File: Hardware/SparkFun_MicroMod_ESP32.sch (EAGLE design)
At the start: 47 parts, among them J1 MICROMOD-2222, Q2 MBT3904DW1T1, U1 W25QXX128MBIT-6X5, U2 ESP32, U4 CP2102N, Y1 40MHz, Y2 32.768kHz

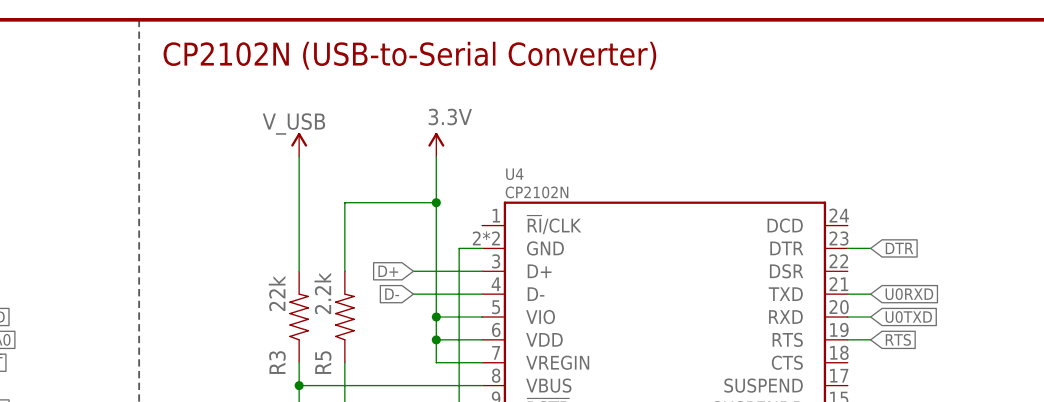
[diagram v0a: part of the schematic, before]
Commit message: Updated USB to UART
USB to UART converter can be either the CP2102N or CP2104
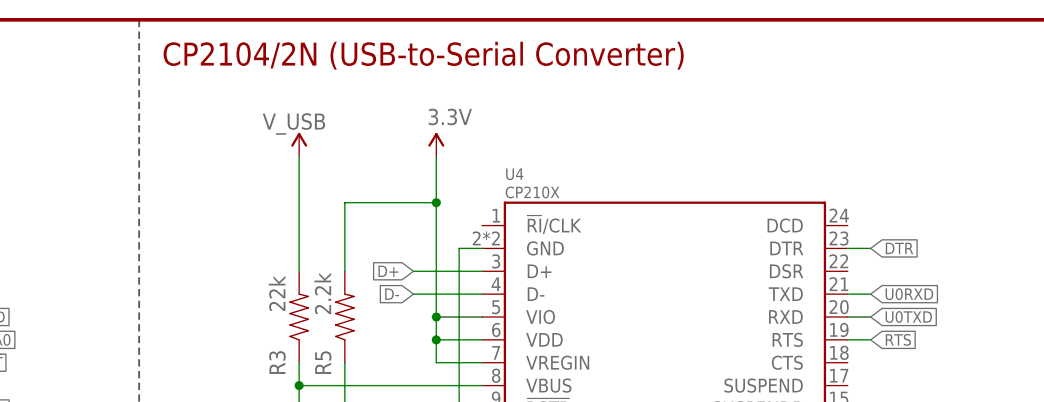
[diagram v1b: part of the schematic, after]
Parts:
- U4: value CP2102N -> CP210X
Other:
- note added: "CP2104/2N (USB-to-Serial Converter)"
- note removed: "CP2102N (USB-to-Serial Converter)"
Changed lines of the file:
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@@
 <?xml version="1.0" encoding="utf-8"?>
 <!DOCTYPE eagle SYSTEM "eagle.dtd">
-<eagle version="9.6.2">
+<eagle version="9.5.2">
 <drawing>
 <settings>
@@
 <layer number="255" name="routoute" color="7" fill="1" visible="yes" active="yes"/>
 </layers>
-<schematic xreflabel="%F%N/%S" xrefpart="1_/%S.%C%R">
+<schematic xreflabel="%F%N/%S" xrefpart="/%S.%C%R">
 <attributes>
 </attributes>
@@
 <part name="C27" library="SparkFun-Capacitors" deviceset="3.0NF" device="-0402T-50V-5%" value="3.0nF"/>
 <part name="GND40" library="SparkFun-PowerSymbols" deviceset="GND" device=""/>
-<part name="U4" library="SparkFun-IC-Comms" deviceset="CP2102N" device=""/>
+<part name="U4" library="SparkFun-IC-Comms" deviceset="CP2102N" device="" value="CP210X"/>
 <part name="GND1" library="SparkFun-PowerSymbols" deviceset="GND" device=""/>
 <part name="SUPPLY5" library="SparkFun-PowerSymbols" deviceset="3.3V" device=""/>
@@
 <text x="381" y="114.3" size="1.778" layer="97" font="vector" align="top-center">If DTR is LOW, toggling RTS from HIGH to LOW resets to run mode.
 If RTS is HIGH, toggling DTR from LOW to HIGH resets to bootloader.</text>
-<text x="332.74" y="274.32" size="2.54" layer="94" font="vector">CP2102N (USB-to-Serial Converter)</text>
+<text x="332.74" y="274.32" size="2.54" layer="94" font="vector">CP2104/2N (USB-to-Serial Converter)</text>
 <text x="200.66" y="274.32" size="2.54" layer="94" font="vector">MicroMod Connector</text>
 <wire x1="198.12" y1="279.4" x2="198.12" y2="193.04" width="0.2032" layer="97" style="longdash"/>

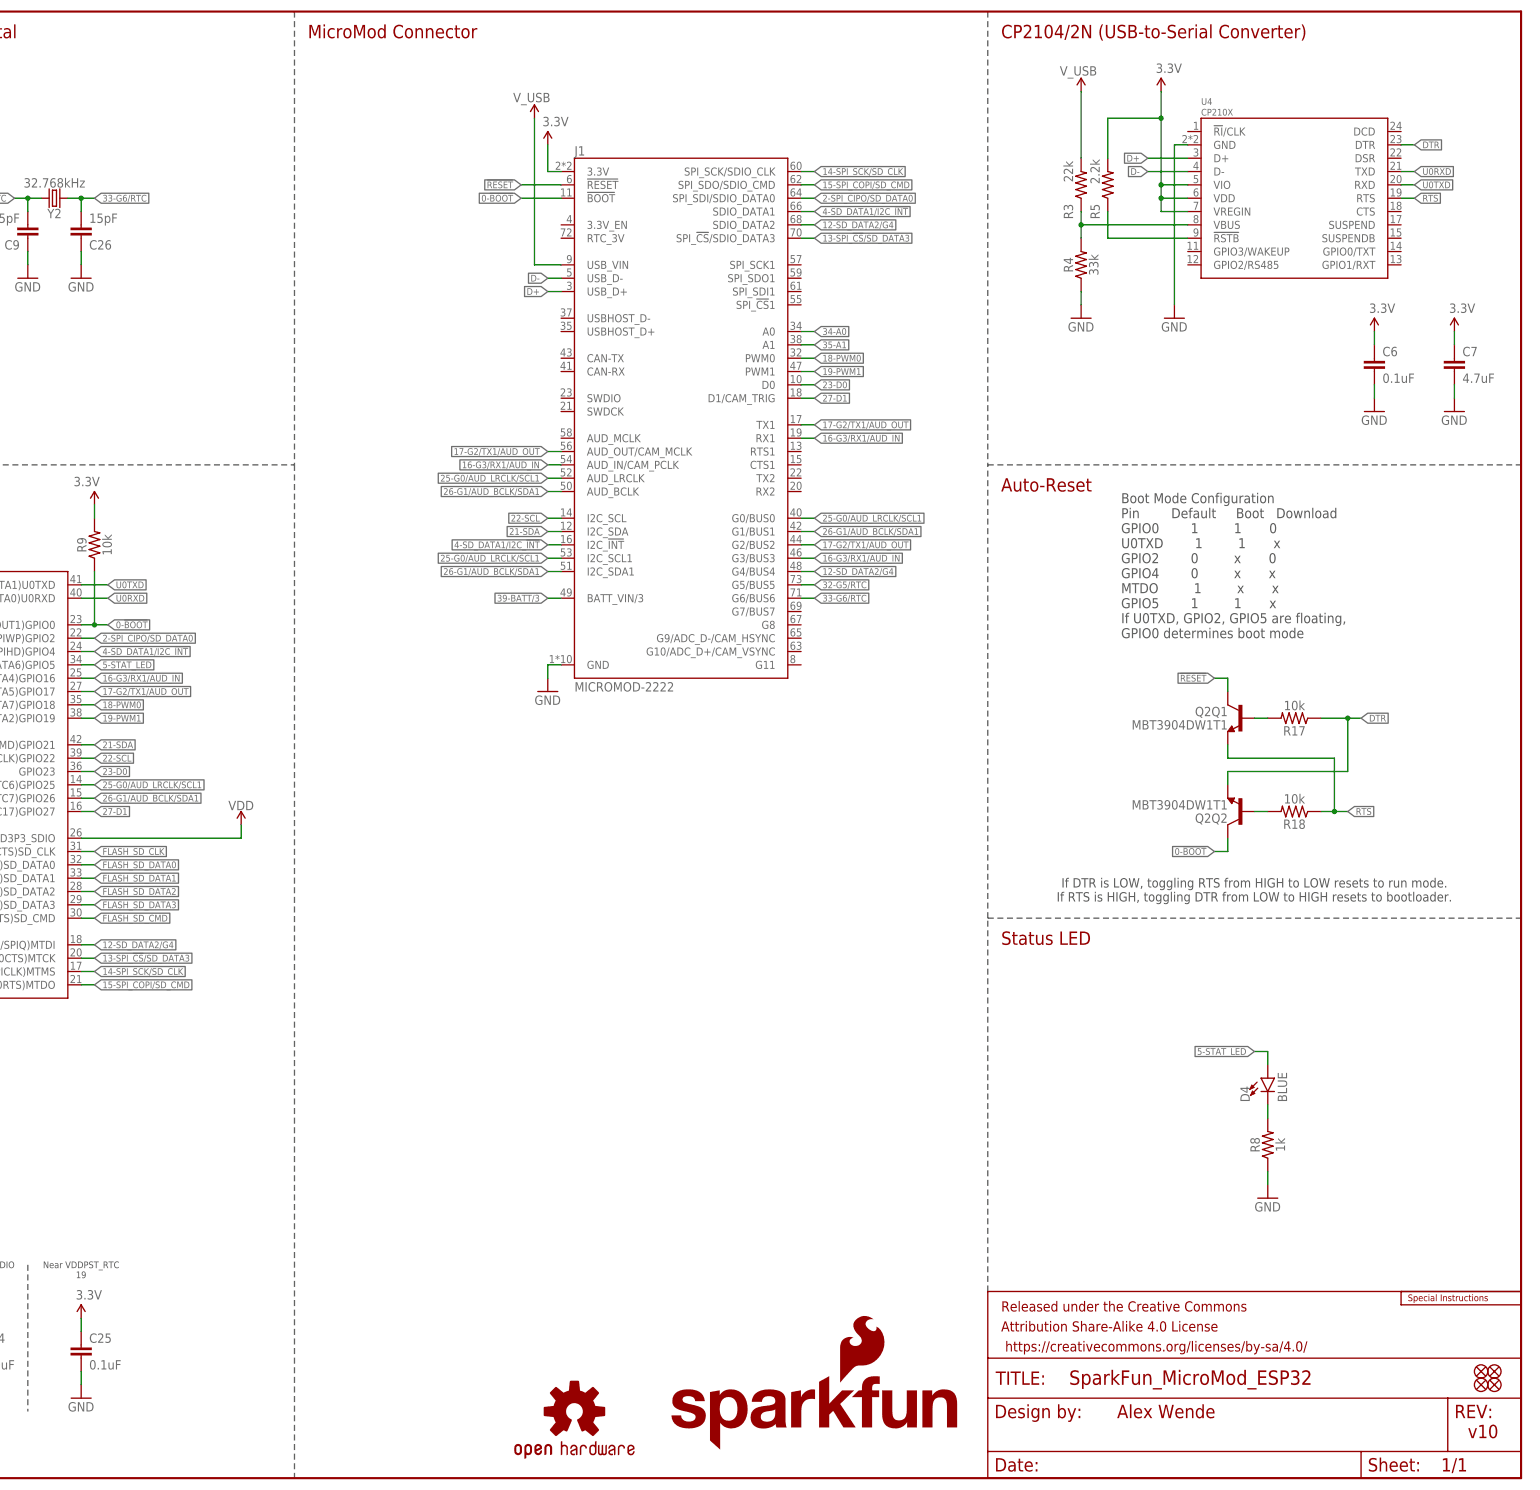
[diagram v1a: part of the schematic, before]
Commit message: v11
- Updated to new MicroMod Pinout
- Changed SCK from 14 to 18
- Changed SDO from 15 to 23
- Changed SDI from 2 to 19
- Changed CS from 13 to 5

- Changed PWM0 from 18 to 13
- Changed PWM1 from 19 to 12
- Changed D0 from 23 to 14

- Updated G0-G4 (mainly just changed GPIO12 to GPIO15, and moved that IO pin G4 to G0 and pushed the other IO pins down one position.
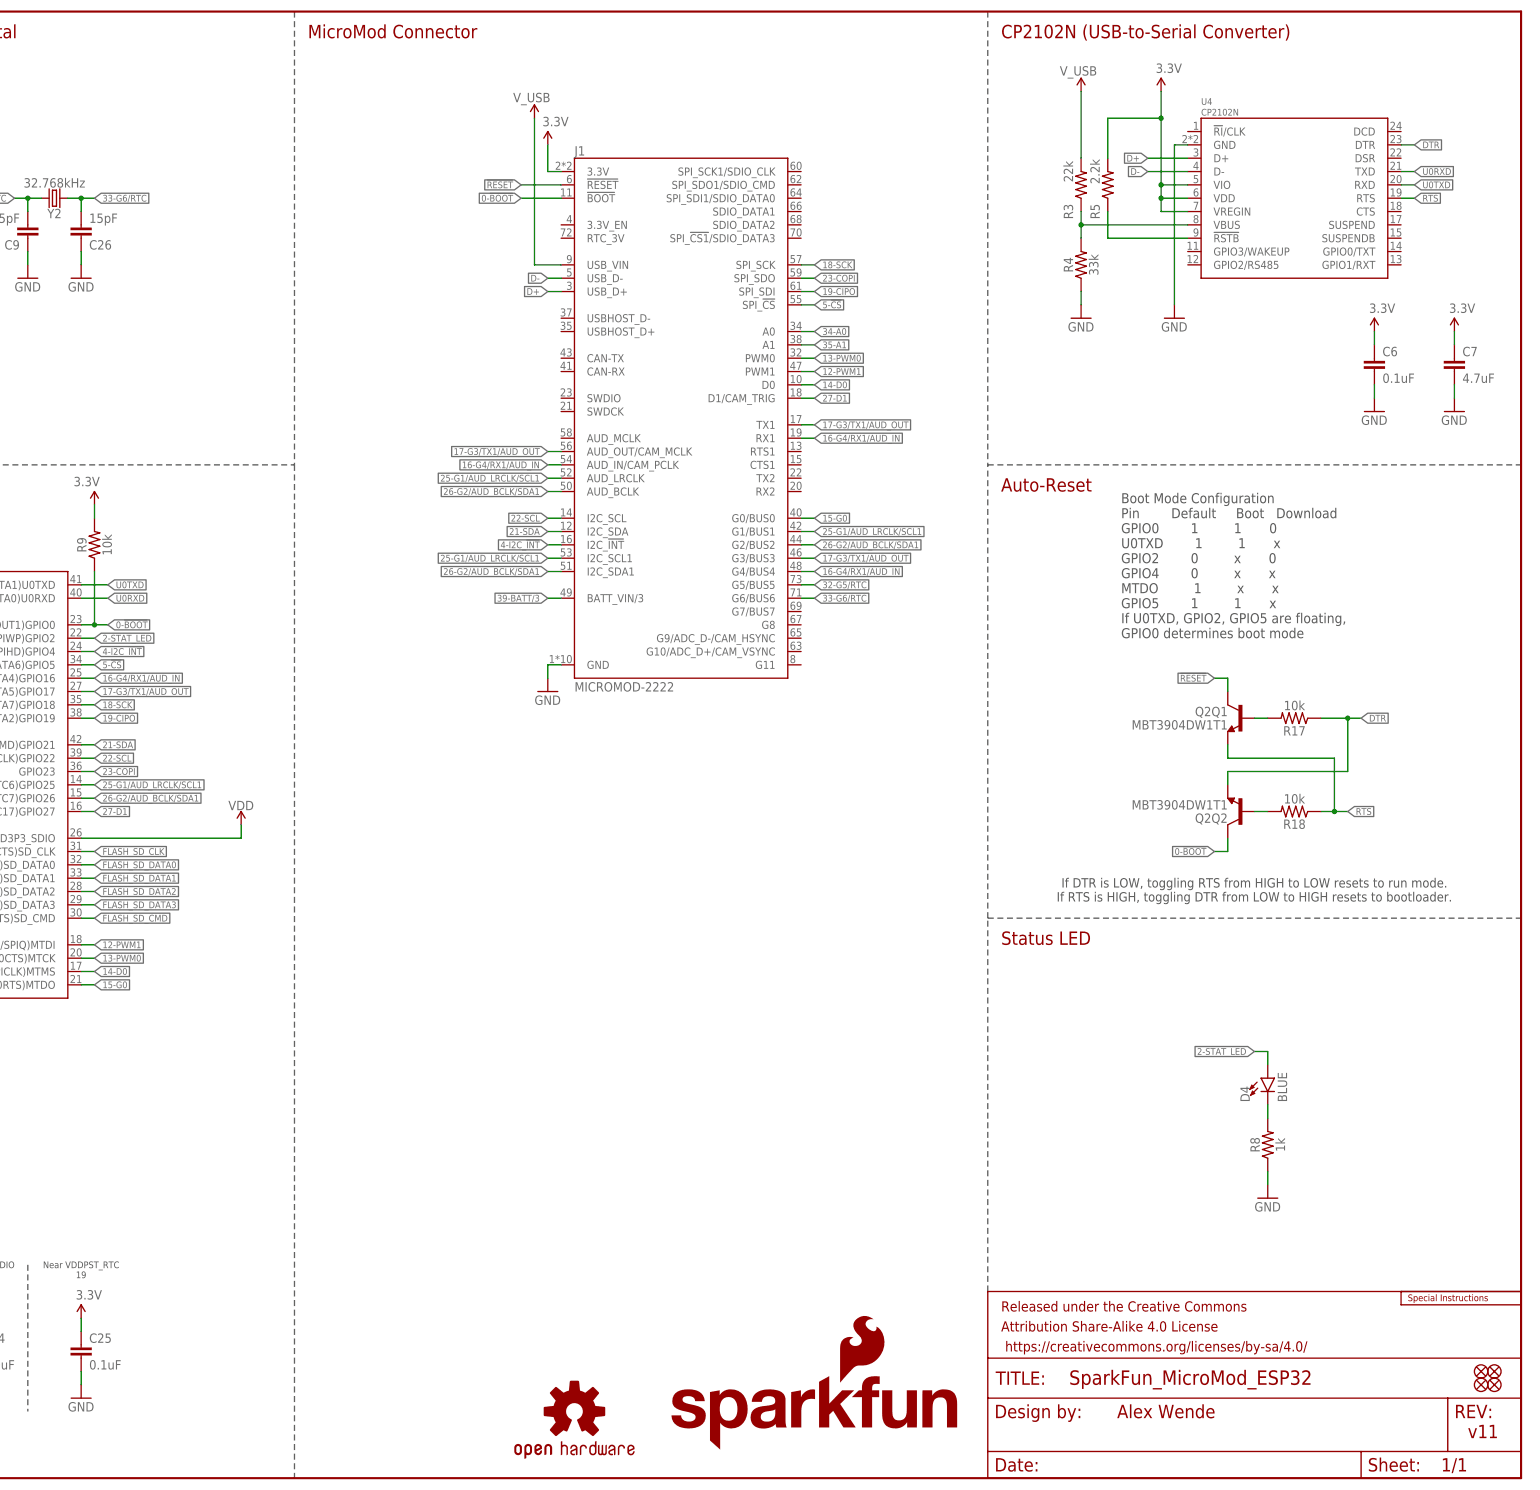
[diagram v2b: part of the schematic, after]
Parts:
- U4: value CP210X -> CP2102N
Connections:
- removed net 12-SD_DATA2/G4: J1.G4/BUS4, J1.SDIO_DATA2, U2.(GPIO12/ADC2:5/TOUCH5/RTC15/SPIQ)MTDI
- removed net 13-SPI_!CS!/SD_DATA3: J1.SPI_!CS!/SDIO_DATA3, U2.(GPIO13/ADC2:4/TOUCH4/RTC14/SPID/U0CTS)MTCK
- removed net 14-SPI_SCK/SD_CLK: J1.SPI_SCK/SDIO_CLK, U2.(GPIO14/ADC2:6/TOUCH6/RTC16/SPICLK)MTMS
- removed net 15-SPI_COPI/SD_CMD: J1.SPI_SDO/SDIO_CMD, U2.(GPIO15/ADC2:3/TOUCH3/RTC13/SPICSO/U0RTS)MTDO
- removed net 16-G3/RX1/AUD_IN: J1.AUD_IN/CAM_PCLK, J1.G3/BUS3, J1.RX1, U2.(HS1_DATA4)GPIO16
- removed net 17-G2/TX1/AUD_OUT: J1.AUD_OUT/CAM_MCLK, J1.G2/BUS2, J1.TX1, U2.(HS1_DATA5)GPIO17
- removed net 18-PWM0: J1.PWM0, U2.(VSPICLK/HS1_DATA7)GPIO18
- removed net 19-PWM1: J1.PWM1, U2.(VSPIQ/HS2_DATA2)GPIO19
- removed net 2-SPI_CIPO/SD_DATA0: J1.SPI_SDI/SDIO_DATA0, U2.(ADC2:2/TOUCH2/RTC12/SPIWP)GPIO2
- removed net 23-D0: J1.D0, U2.GPIO23
- removed net 25-G0/AUD_LRCLK/SCL1: J1.AUD_LRCLK, J1.G0/BUS0, J1.I2C_SCL1, U2.(DAC1/ADC2:8/RTC6)GPIO25
- removed net 26-G1/AUD_BCLK/SDA1: J1.AUD_BCLK, J1.G1/BUS1, J1.I2C_SDA1, U2.(DAC2/ADC2:9/RTC7)GPIO26
- removed net 4-SD_DATA1/I2C_!INT: J1.I2C_!INT!, J1.SDIO_DATA1, U2.(ADC2:0/TOUCH0/RTC10/SPIHD)GPIO4
- removed net 5-STAT_LED: D4.A, U2.(VSPICS0/HS1_DATA6)GPIO5
- new net 12-PWM1: J1.PWM1, U2.(GPIO12/ADC2:5/TOUCH5/RTC15/SPIQ)MTDI
- new net 13-PWM0: J1.PWM0, U2.(GPIO13/ADC2:4/TOUCH4/RTC14/SPID/U0CTS)MTCK
- new net 14-D0: J1.D0, U2.(GPIO14/ADC2:6/TOUCH6/RTC16/SPICLK)MTMS
- new net 15-G0: J1.G0/BUS0, U2.(GPIO15/ADC2:3/TOUCH3/RTC13/SPICSO/U0RTS)MTDO
- new net 16-G4/RX1/AUD_IN: J1.AUD_IN/CAM_PCLK, J1.G4/BUS4, J1.RX1, U2.(HS1_DATA4)GPIO16
- new net 17-G3/TX1/AUD_OUT: J1.AUD_OUT/CAM_MCLK, J1.G3/BUS3, J1.TX1, U2.(HS1_DATA5)GPIO17
- new net 18-SCK: J1.SPI_SCK, U2.(VSPICLK/HS1_DATA7)GPIO18
- new net 19-CIPO: J1.SPI_SDI, U2.(VSPIQ/HS2_DATA2)GPIO19
- new net 2-STAT_LED: D4.A, U2.(ADC2:2/TOUCH2/RTC12/SPIWP)GPIO2
- new net 23-COPI: J1.SPI_SDO, U2.GPIO23
- new net 25-G1/AUD_LRCLK/SCL1: J1.AUD_LRCLK, J1.G1/BUS1, J1.I2C_SCL1, U2.(DAC1/ADC2:8/RTC6)GPIO25
- new net 26-G2/AUD_BCLK/SDA1: J1.AUD_BCLK, J1.G2/BUS2, J1.I2C_SDA1, U2.(DAC2/ADC2:9/RTC7)GPIO26
- new net 4-I2C_!INT: J1.I2C_!INT!, U2.(ADC2:0/TOUCH0/RTC10/SPIHD)GPIO4
- new net 5-!CS: J1.SPI_!CS!, U2.(VSPICS0/HS1_DATA6)GPIO5
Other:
- note added: "CP2102N (USB-to-Serial Converter)"
- note added: "v11"
- note removed: "CP2104/2N (USB-to-Serial Converter)"
- note removed: "v10"

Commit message: v11 update
- Added notes to boot strapping pins
- Added ENIG finish note to tDocu
- Updated labeling for USB to UART brdige
- Updated SPI flash labels
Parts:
- U4: value CP2102N -> CP210X
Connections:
- net FLASH_SD_CLK renamed FLASH_SCK
- net FLASH_SD_CMD renamed FLASH_SCS
- net FLASH_SD_DATA0 renamed FLASH_SDO
- net FLASH_SD_DATA1 renamed FLASH_SDI
- net FLASH_SD_DATA2 renamed FLASH_SHD
- net FLASH_SD_DATA3 renamed FLASH_SWP
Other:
- note added: "CP2104/2N (USB-to-Serial Converter)"
- note added: "GPIO2 must be able to be driven low to enter bootloader"
- note added: "Pulling GPIO12 high may prevent flashing and/or booting"
- note added: "Pulling GPIO15 high will silence boot messages printed by the bootloader"
- note removed: "CP2102N (USB-to-Serial Converter)"
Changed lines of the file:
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@@
 <?xml version="1.0" encoding="utf-8"?>
 <!DOCTYPE eagle SYSTEM "eagle.dtd">
-<eagle version="9.6.2">
+<eagle version="9.5.2">
 <drawing>
 <settings>
@@
 <layer number="255" name="routoute" color="7" fill="1" visible="yes" active="yes"/>
 </layers>
-<schematic xreflabel="%F%N/%S" xrefpart="1_/%S.%C%R">
+<schematic xreflabel="%F%N/%S" xrefpart="/%S.%C%R">
 <attributes>
 </attributes>
@@
 <part name="C27" library="SparkFun-Capacitors" deviceset="3.0NF" device="-0402T-50V-5%" value="3.0nF"/>
 <part name="GND40" library="SparkFun-PowerSymbols" deviceset="GND" device=""/>
-<part name="U4" library="SparkFun-IC-Comms" deviceset="CP2102N" device=""/>
+<part name="U4" library="SparkFun-IC-Comms" deviceset="CP2102N" device="" value="CP210X"/>
 <part name="GND1" library="SparkFun-PowerSymbols" deviceset="GND" device=""/>
 <part name="SUPPLY5" library="SparkFun-PowerSymbols" deviceset="3.3V" device=""/>
@@
 <text x="381" y="114.3" size="1.778" layer="97" font="vector" align="top-center">If DTR is LOW, toggling RTS from HIGH to LOW resets to run mode.
 If RTS is HIGH, toggling DTR from LOW to HIGH resets to bootloader.</text>
-<text x="332.74" y="274.32" size="2.54" layer="94" font="vector">CP2102N (USB-to-Serial Converter)</text>
+<text x="332.74" y="274.32" size="2.54" layer="94" font="vector">CP2104/2N (USB-to-Serial Converter)</text>
 <text x="200.66" y="274.32" size="2.54" layer="94" font="vector">MicroMod Connector</text>
 <wire x1="198.12" y1="279.4" x2="198.12" y2="193.04" width="0.2032" layer="97" style="longdash"/>
@@
 RF Trace Width: 13mil/0.3302mm</text>
 <text x="91.44" y="58.42" size="0.8128" layer="97" font="vector">https://chemandy.com/calculators/coplanar-waveguide-with-ground-calculator.htm</text>
+<text x="175.26" y="157.48" size="1.27" layer="97" font="vector">GPIO2 must be able
+to be driven low to
+enter bootloader</text>
+<text x="172.72" y="99.06" size="1.27" layer="97" font="vector">Pulling GPIO12 high
+may prevent flashing
+and/or booting</text>
+<text x="172.72" y="86.36" size="1.27" layer="97" font="vector">Pulling GPIO15 high
+will silence boot
+messages printed
+by the bootloader</text>
 </plain>
 <instances>
@@
 </segment>
 </net>
-<net name="FLASH_SD_DATA3" class="0">
+<net name="FLASH_SWP" class="0">
 <segment>
 <wire x1="157.48" y1="109.22" x2="160.02" y2="109.22" width="0.1524" layer="91"/>
@@
 </segment>
 </net>
-<net name="FLASH_SD_DATA2" class="0">
+<net name="FLASH_SHD" class="0">
 <segment>
 <wire x1="157.48" y1="111.76" x2="160.02" y2="111.76" width="0.1524" layer="91"/>
@@
 </segment>
 </net>
-<net name="FLASH_SD_DATA1" class="0">
+<net name="FLASH_SDI" class="0">
 <segment>
 <wire x1="157.48" y1="114.3" x2="160.02" y2="114.3" width="0.1524" layer="91"/>
@@
 </segment>
 </net>
-<net name="FLASH_SD_DATA0" class="0">
+<net name="FLASH_SDO" class="0">
 <segment>
 <wire x1="157.48" y1="116.84" x2="160.02" y2="116.84" width="0.1524" layer="91"/>
@@
 </segment>
 </net>
-<net name="FLASH_SD_CLK" class="0">
+<net name="FLASH_SCK" class="0">
 <segment>
 <wire x1="157.48" y1="119.38" x2="160.02" y2="119.38" width="0.1524" layer="91"/>
@@
 </segment>
 </net>
-<net name="FLASH_SD_CMD" class="0">
+<net name="FLASH_SCS" class="0">
 <segment>
 <wire x1="157.48" y1="106.68" x2="160.02" y2="106.68" width="0.1524" layer="91"/>
